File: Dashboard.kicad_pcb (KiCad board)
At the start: 2 copper layers, 176.5 x 121.5 mm, 161 parts, among them J1 Left_Signal, J10 AccelConn, J11 BrakeConn, J12 AccelConn2, J13 BrakeConn2, J14 Motor-P, J15 Motor-C, J16 Array-C, J17 Array-P, J18 PowerConn, J19 CAN_OUT, J2 Right_Signal, J20 MotorCANConnector, J21 CAN_IN, J22 CAN_OUT, J23 USB_B_Micro, J24 ExtraGPIO_Conn, J25 UART_TP, J26 CAN_TP, J27 CAN_TP, J28 KILL_SW_IND, J3 Brake Light, J4 Headlight, J5 MinionConn, J6 SPI, J7 BPS_PWR_OUT, J8 JTAG, J9 POW_2ND_CONN, SW10 RESET, SW8 SW_Rotary2x6, U1 EL3H7, U10 EL3H7, U11 EL3H7, U12 RI3-1205S, U13 NCP1117-3.3_SOT223, U14 ADM3055E, U15 CDSOT23-T24CAN, U16 LTC6820, U17 ADM3055E, U18 CDSOT23-T24CAN, U19 CP2102N-A01-GQFN24, U2 EL3H7, U20 HX1188FNL, U3 EL3H7, U4 EL3H7, U5 EL3H7, U6 EL3H7, U7 STM32F413RHTx, U8 EL3H7, U9 EL3H7, Y1 Crystal

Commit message: Add STEP file
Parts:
- R13, R14, R19, R20: value ? -> 5.1k
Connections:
- J23 pad 4: Net-(J23-Pad4) -> (no net)
- J5 pad 11: Net-(J5-Pad11) -> (no net)
- J5 pad 12: Net-(J5-Pad12) -> (no net)
- J5 pad 5: Net-(J5-Pad5) -> (no net)
- J5 pad 6: Net-(J5-Pad6) -> (no net)
- PS1 pad 2: Net-(PS1-Pad2) -> (no net)
- PS2 pad 2: Net-(PS2-Pad2) -> (no net)
- PS3 pad 2: Net-(PS3-Pad2) -> (no net)
- PS4 pad 2: Net-(PS4-Pad2) -> (no net)
- SW8 pad 12: Net-(SW8-Pad12) -> (no net)
- SW8 pad 6: Net-(SW8-Pad6) -> (no net)
- U14 pad 17: Net-(U14-Pad17) -> (no net)
- U14 pad 6: Net-(U14-Pad6) -> (no net)
- U14 pad 8: Net-(U14-Pad8) -> (no net)
- U14 pad 9: Net-(U14-Pad9) -> (no net)
- U17 pad 17: Net-(U17-Pad17) -> (no net)
- U17 pad 6: Net-(U17-Pad6) -> (no net)
- U17 pad 8: Net-(U17-Pad8) -> (no net)
- U17 pad 9: Net-(U17-Pad9) -> (no net)
- U19 pad 1: Net-(U19-Pad1) -> (no net)
- U19 pad 10: Net-(U19-Pad10) -> (no net)
- U19 pad 11: Net-(U19-Pad11) -> (no net)
- U19 pad 12: Net-(U19-Pad12) -> (no net)
- U19 pad 13: Net-(U19-Pad13) -> (no net)
- U19 pad 14: Net-(U19-Pad14) -> (no net)
- U19 pad 15: Net-(U19-Pad15) -> (no net)
- U19 pad 16: Net-(U19-Pad16) -> (no net)
- U19 pad 17: Net-(U19-Pad17) -> (no net)
- U19 pad 18: Net-(U19-Pad18) -> (no net)
- U19 pad 19: Net-(U19-Pad19) -> (no net)
- U19 pad 22: Net-(U19-Pad22) -> (no net)
- U19 pad 23: Net-(U19-Pad23) -> (no net)
- U19 pad 24: Net-(U19-Pad24) -> (no net)
- U20 pad 10: Net-(U20-Pad10) -> (no net)
- U20 pad 11: Net-(U20-Pad11) -> (no net)
- U20 pad 15: Net-(U20-Pad15) -> (no net)
- U20 pad 2: Net-(U20-Pad2) -> (no net)
- U20 pad 6: Net-(U20-Pad6) -> (no net)
- U20 pad 7: Net-(U20-Pad7) -> (no net)
- U20 pad 8: Net-(U20-Pad8) -> (no net)
- U20 pad 9: Net-(U20-Pad9) -> (no net)
- U7 pad 24: Net-(U7-Pad24) -> (no net)
- U7 pad 26: Net-(U7-Pad26) -> (no net)
- U7 pad 27: Net-(U7-Pad27) -> (no net)
- U7 pad 28: Net-(U7-Pad28) -> (no net)
- U7 pad 35: Net-(U7-Pad35) -> (no net)
- U7 pad 36: Net-(U7-Pad36) -> (no net)
- U7 pad 41: Net-(U7-Pad41) -> (no net)
- U7 pad 42: Net-(U7-Pad42) -> (no net)
- U7 pad 43: Net-(U7-Pad43) -> (no net)
- U7 pad 61: Net-(U7-Pad61) -> (no net)
- U7 pad 62: Net-(U7-Pad62) -> (no net)

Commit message: Updates Controls Leader PCB
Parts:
- D1: moved to B.Cu
- moved D1 3.00 mm to (202.5, 142.7), turned to 270 degrees
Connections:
- J23 pad 4: (no net) -> Net-(J23-Pad4)
- J5 pad 1: +3V3 -> +5V
- J5 pad 11: (no net) -> Net-(J5-Pad11)
- J5 pad 12: (no net) -> Net-(J5-Pad12)
- J5 pad 5: (no net) -> /BPS_PWR
- J5 pad 6: (no net) -> Net-(J5-Pad6)
- PS1 pad 2: (no net) -> Net-(PS1-Pad2)
- PS2 pad 2: (no net) -> Net-(PS2-Pad2)
- PS3 pad 2: (no net) -> Net-(PS3-Pad2)
- PS4 pad 2: (no net) -> Net-(PS4-Pad2)
- SW8 pad 12: (no net) -> Net-(SW8-Pad12)
- SW8 pad 6: (no net) -> Net-(SW8-Pad6)
- U14 pad 17: (no net) -> Net-(U14-Pad17)
- U14 pad 6: (no net) -> Net-(U14-Pad6)
- U14 pad 8: (no net) -> Net-(U14-Pad8)
- U14 pad 9: (no net) -> Net-(U14-Pad9)
- U17 pad 17: (no net) -> Net-(U17-Pad17)
- U17 pad 6: (no net) -> Net-(U17-Pad6)
- U17 pad 8: (no net) -> Net-(U17-Pad8)
- U17 pad 9: (no net) -> Net-(U17-Pad9)
- U19 pad 1: (no net) -> Net-(U19-Pad1)
- U19 pad 10: (no net) -> Net-(U19-Pad10)
- U19 pad 11: (no net) -> Net-(U19-Pad11)
- U19 pad 12: (no net) -> Net-(U19-Pad12)
- U19 pad 13: (no net) -> Net-(U19-Pad13)
- U19 pad 14: (no net) -> Net-(U19-Pad14)
- U19 pad 15: (no net) -> Net-(U19-Pad15)
- U19 pad 16: (no net) -> Net-(U19-Pad16)
- U19 pad 17: (no net) -> Net-(U19-Pad17)
- U19 pad 18: (no net) -> Net-(U19-Pad18)
- U19 pad 19: (no net) -> Net-(U19-Pad19)
- U19 pad 22: (no net) -> Net-(U19-Pad22)
- U19 pad 23: (no net) -> Net-(U19-Pad23)
- U19 pad 24: (no net) -> Net-(U19-Pad24)
- U20 pad 10: (no net) -> Net-(U20-Pad10)
- U20 pad 11: (no net) -> Net-(U20-Pad11)
- U20 pad 15: (no net) -> Net-(U20-Pad15)
- U20 pad 2: (no net) -> Net-(U20-Pad2)
- U20 pad 6: (no net) -> Net-(U20-Pad6)
- U20 pad 7: (no net) -> Net-(U20-Pad7)
- U20 pad 8: (no net) -> Net-(U20-Pad8)
- U20 pad 9: (no net) -> Net-(U20-Pad9)
- U7 pad 24: (no net) -> Net-(U7-Pad24)
- U7 pad 26: (no net) -> Net-(U7-Pad26)
- U7 pad 27: (no net) -> Net-(U7-Pad27)
- U7 pad 28: (no net) -> Net-(U7-Pad28)
- U7 pad 35: (no net) -> Net-(U7-Pad35)
- U7 pad 36: (no net) -> Net-(U7-Pad36)
- U7 pad 41: (no net) -> Net-(U7-Pad41)
- U7 pad 42: (no net) -> Net-(U7-Pad42)
- U7 pad 43: (no net) -> Net-(U7-Pad43)
- U7 pad 61: (no net) -> Net-(U7-Pad61)
- U7 pad 62: (no net) -> Net-(U7-Pad62)
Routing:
- net /BPS_PWR: track 92.2 -> 192.2 mm, vias 0 -> 4
- net +5V: track 132.1 -> 163.8 mm
- net +3V3: track 533.1 -> 511.9 mm, vias 26 -> 27
- net Net-(D1-Pad1): track 15.4 -> 12.4 mm
- net Net-(D1-Pad2): track 7.70 -> 9.35 mm
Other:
- board text added: "+5V"
- board text added: "PWR"

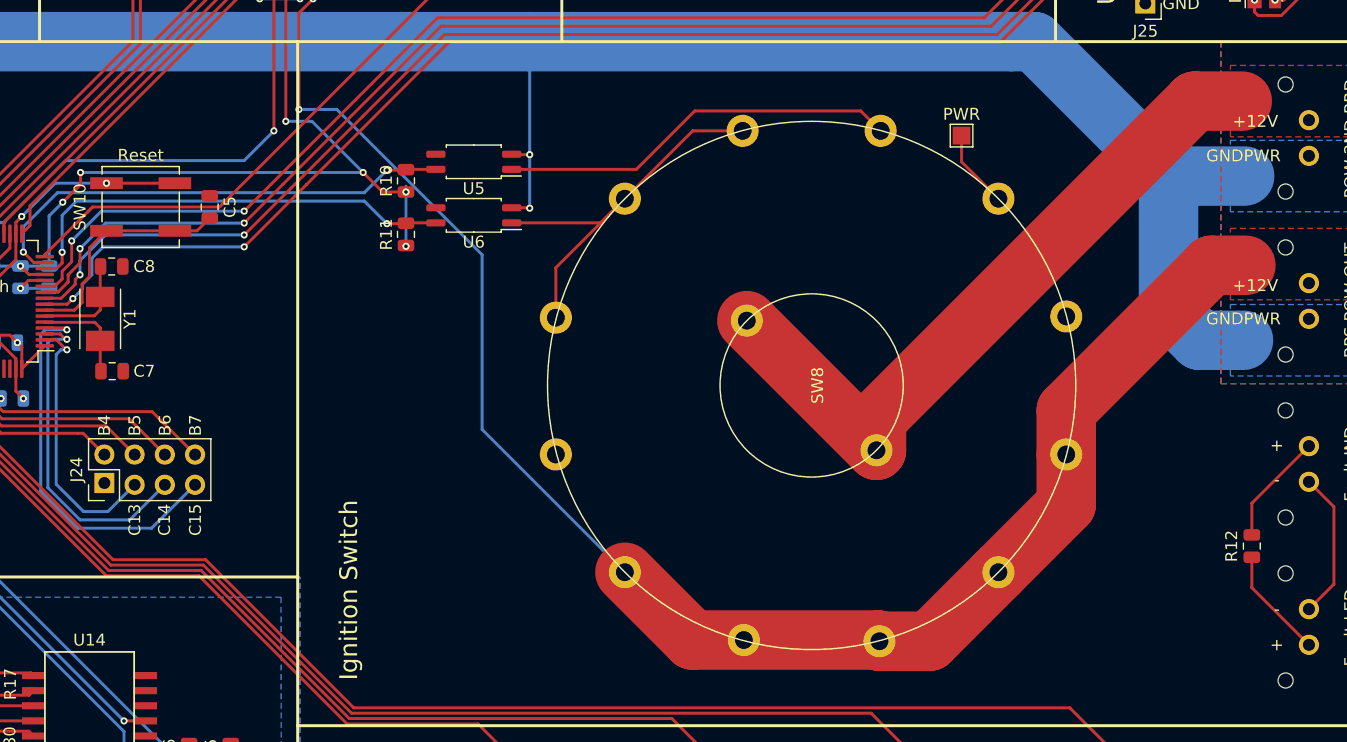
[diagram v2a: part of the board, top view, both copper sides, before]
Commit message: 3D models and resized rotary switch
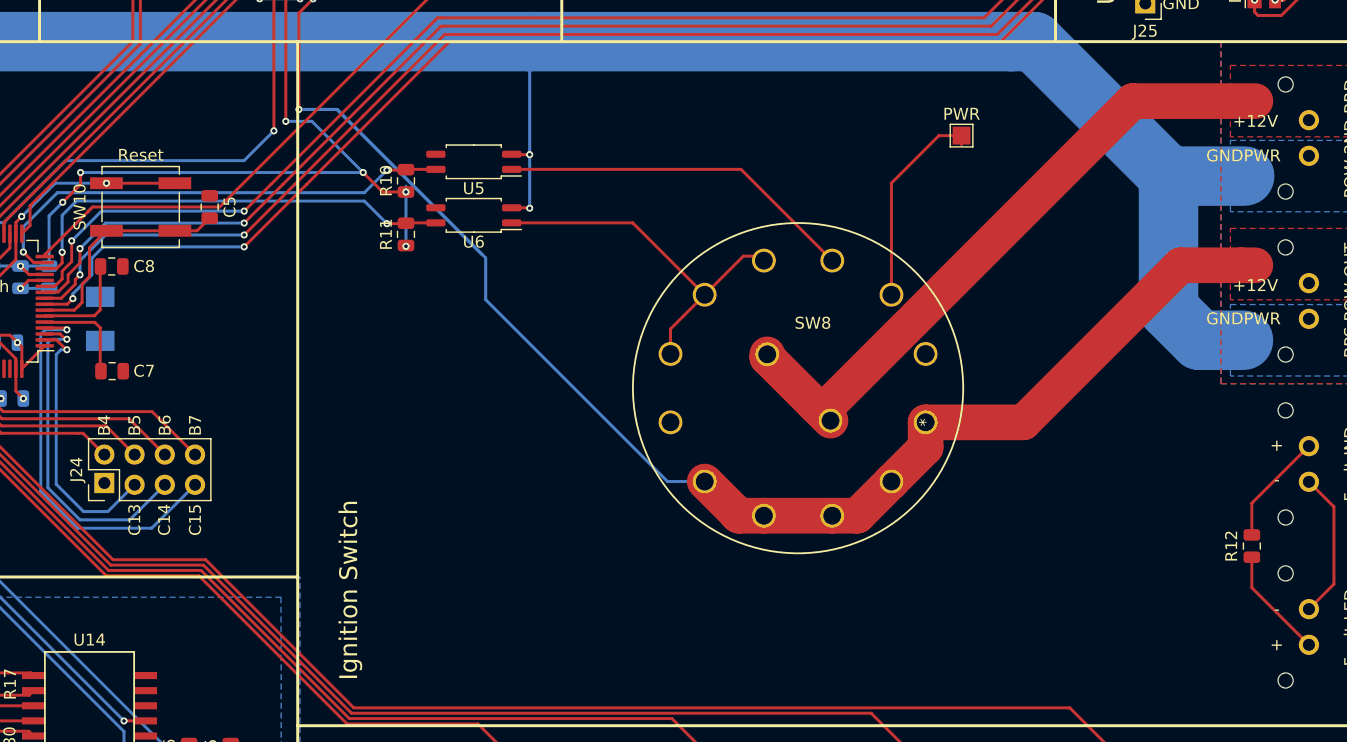
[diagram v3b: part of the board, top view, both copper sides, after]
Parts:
- SW8: footprint UTSVT_Special:CK1035 -> UTSVT_Special:CK1035_resized
- Y1: moved to B.Cu
- moved SW8 10.1 mm to (170.3, 127.0)
- turned Y1 to 90 degrees
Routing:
- net /BPS_PWR: track 192.2 -> 174.9 mm
- net Net-(SW8-Pad11): track 6.58 -> 17.7 mm
- net Net-(J9-Pad1): track 59.8 -> 55.4 mm
- net Net-(SW8-Pad7): track 35.0 -> 31.4 mm
- net Net-(SW8-Pad10): track 33.7 -> 30.1 mm

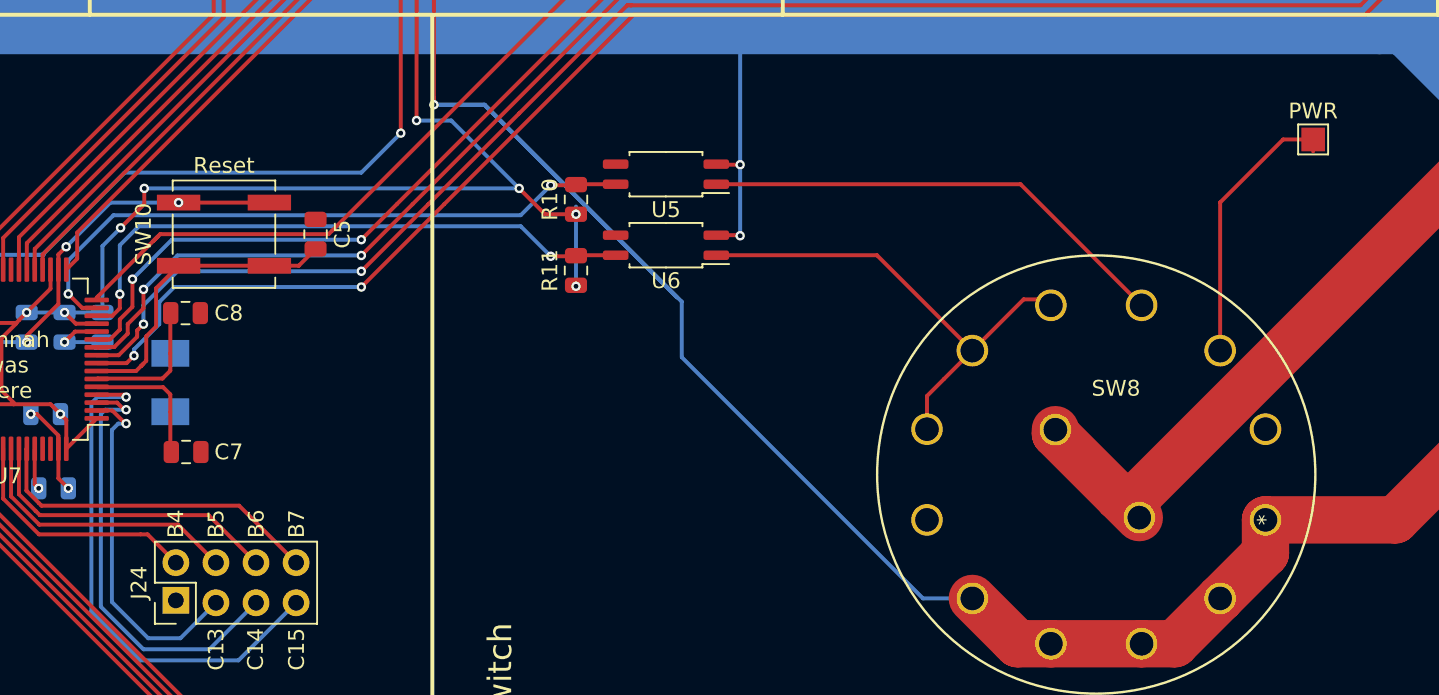
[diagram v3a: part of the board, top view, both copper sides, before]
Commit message: Cleans up folder and updates gerbers
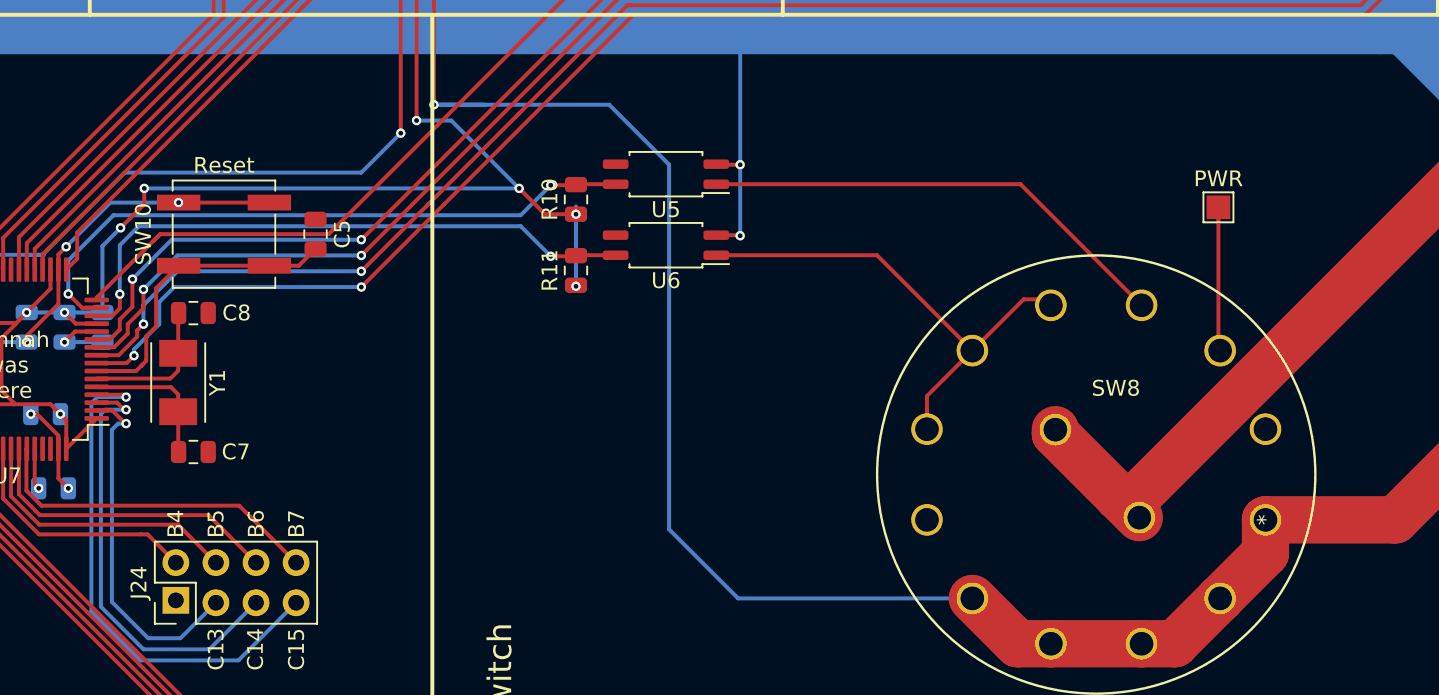
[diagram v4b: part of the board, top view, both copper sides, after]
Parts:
- Y1: moved to F.Cu
- moved TP10 7.38 mm to (167.3, 107.2)
- moved C8 0.50 mm to (102.4, 113.9)
- moved Y1 0.50 mm to (101.4, 118.3), turned to 270 degrees
- moved C7 0.46 mm to (102.4, 122.7)
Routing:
- net Net-(SW8-Pad11): track 17.7 -> 9.88 mm
- net /BPS_PWR: track 174.9 -> 169.1 mm
- net Net-(C7-Pad1): track 8.54 -> 9.04 mm
- net Net-(C8-Pad1): track 8.54 -> 9.04 mm

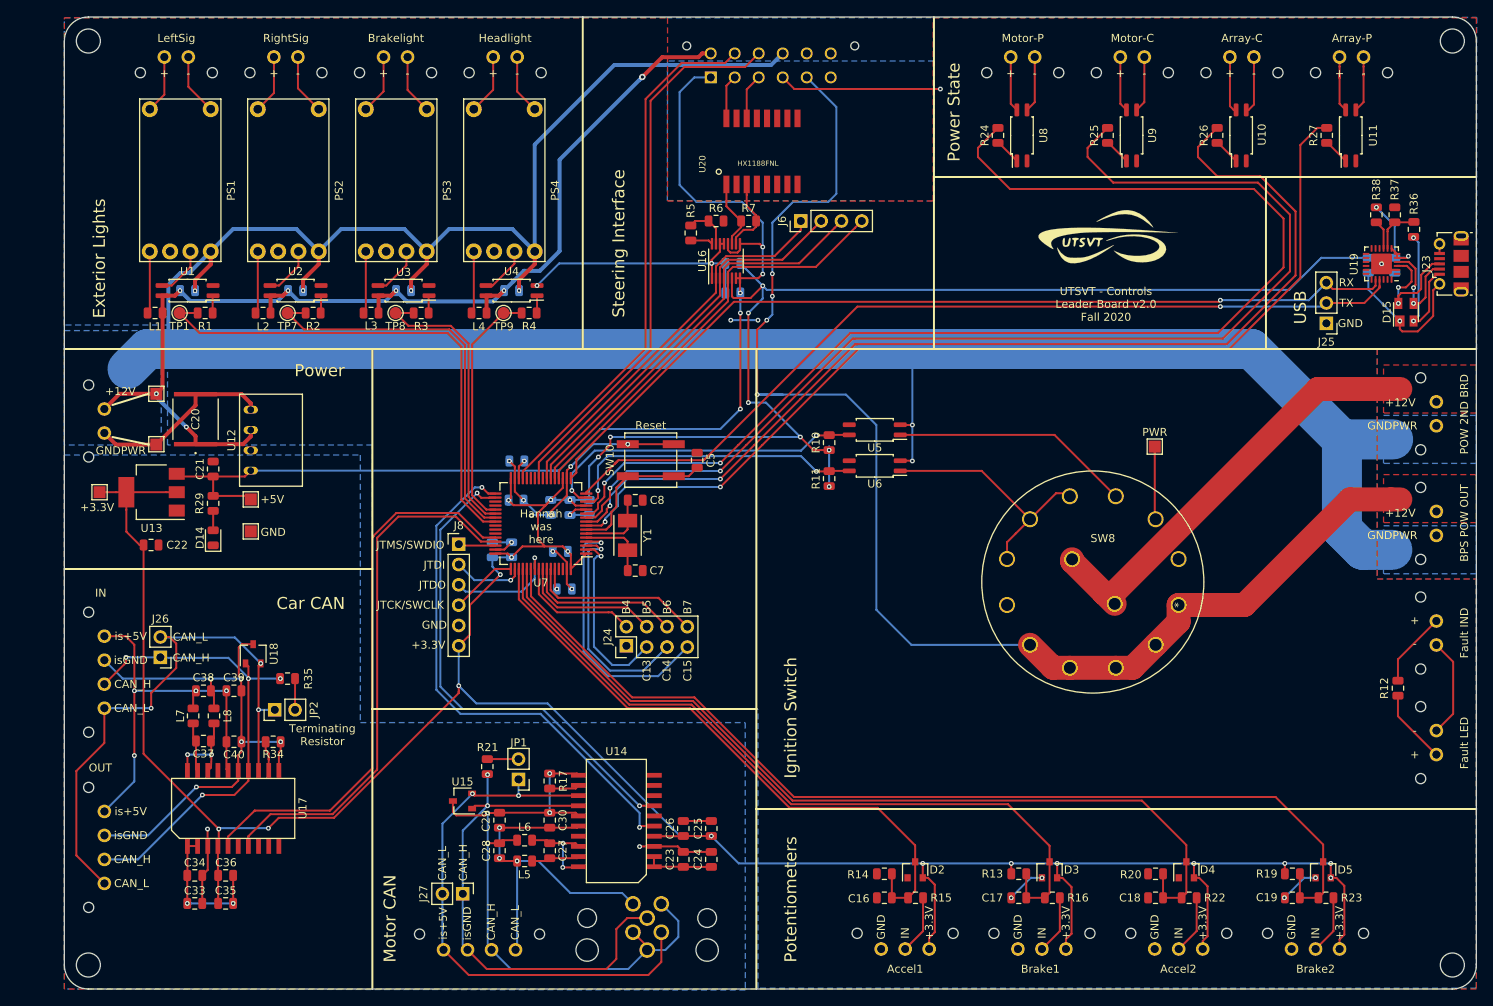
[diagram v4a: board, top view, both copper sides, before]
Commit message: USB Tx/Rx, Crystal Keepout, 12V Separation, Can2-Can3, Motor CAN bus labels, Power Input Protection Circuitry
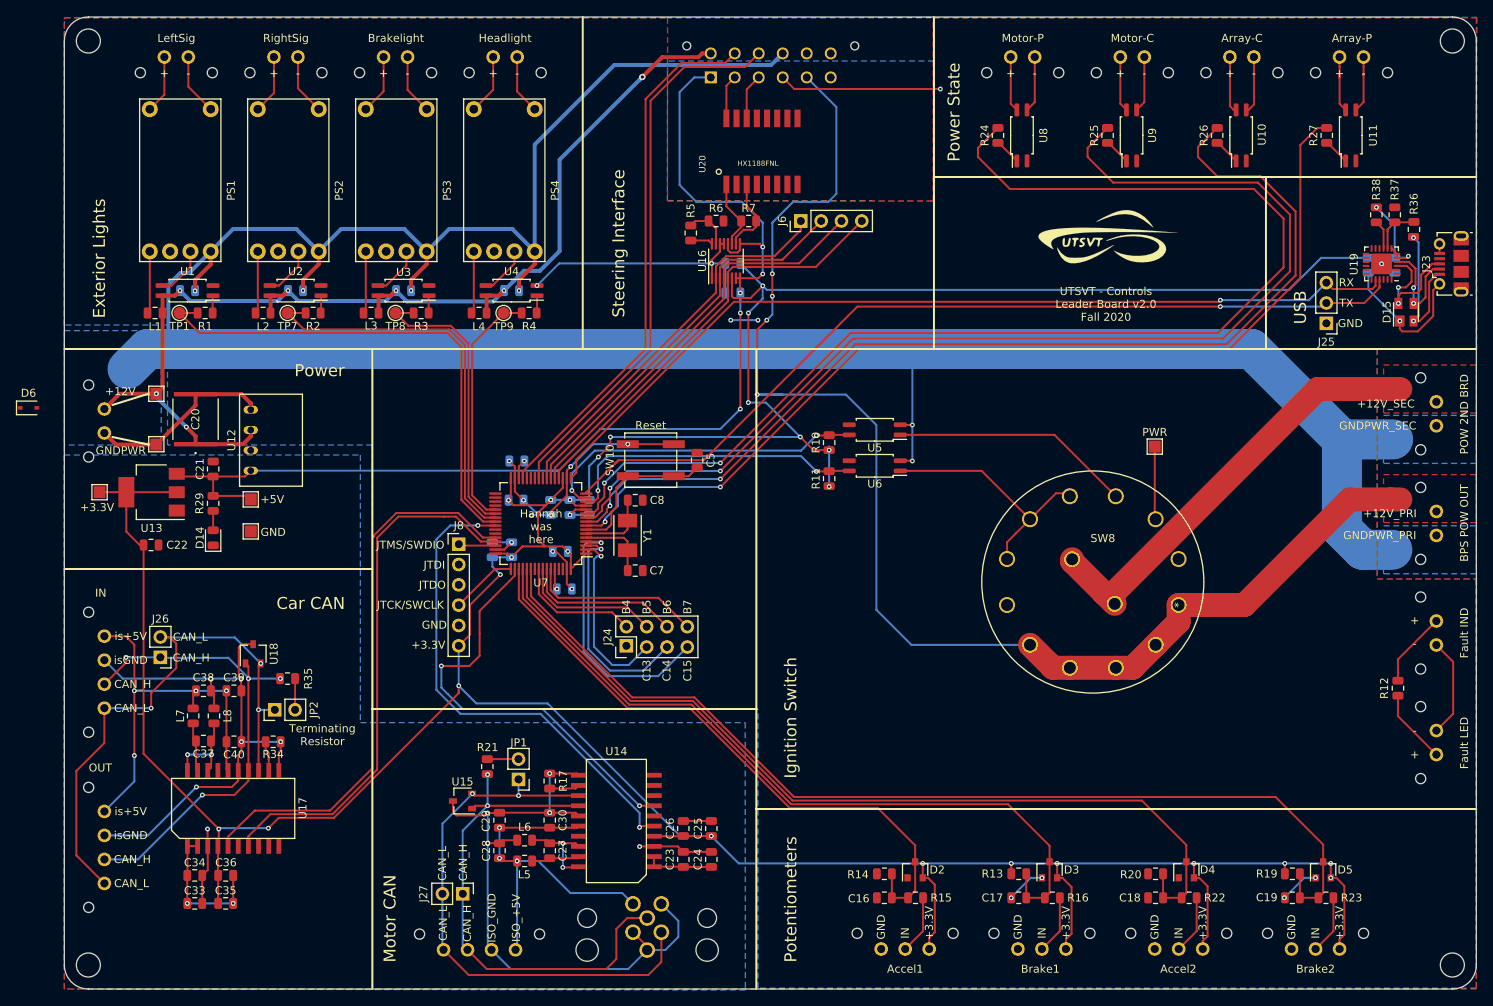
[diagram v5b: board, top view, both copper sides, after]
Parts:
- added D6: TVS, Diode_SMD:D_SOD-323, F.Cu at (26.5, 102.4)
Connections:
- U19 pad 20: /UART2_Rx -> /UART2_Tx
- U19 pad 21: /UART2_Tx -> /UART2_Rx
- U7 pad 33: /MotorCAN_Rx -> Net-(U7-Pad33)
- U7 pad 34: /MotorCAN_Tx -> Net-(U7-Pad34)
- U7 pad 41: Net-(U7-Pad41) -> /MotorCAN_Rx
- U7 pad 50: /JTDI -> /MotorCAN_Tx
- U7 pad 55: /JTDO -> Net-(U7-Pad55)
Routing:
- net /JTDO: track 14.5 -> 0.00 mm, vias 1 -> 0
- net /JTDI: track 8.93 -> 0.00 mm, vias 1 -> 0
- net /MotorCAN_Tx: track 61.6 -> 53.4 mm
- net /MotorCAN_Rx: track 65.6 -> 62.4 mm
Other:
- board text added: "+12V_PRI"
- board text added: "+12V_SEC"
- board text added: "GNDPWR_PRI"
- board text added: "GNDPWR_SEC"
- board text added: "ISO_+5V"
- board text added: "ISO_GND"
